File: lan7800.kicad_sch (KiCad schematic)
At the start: 31 parts

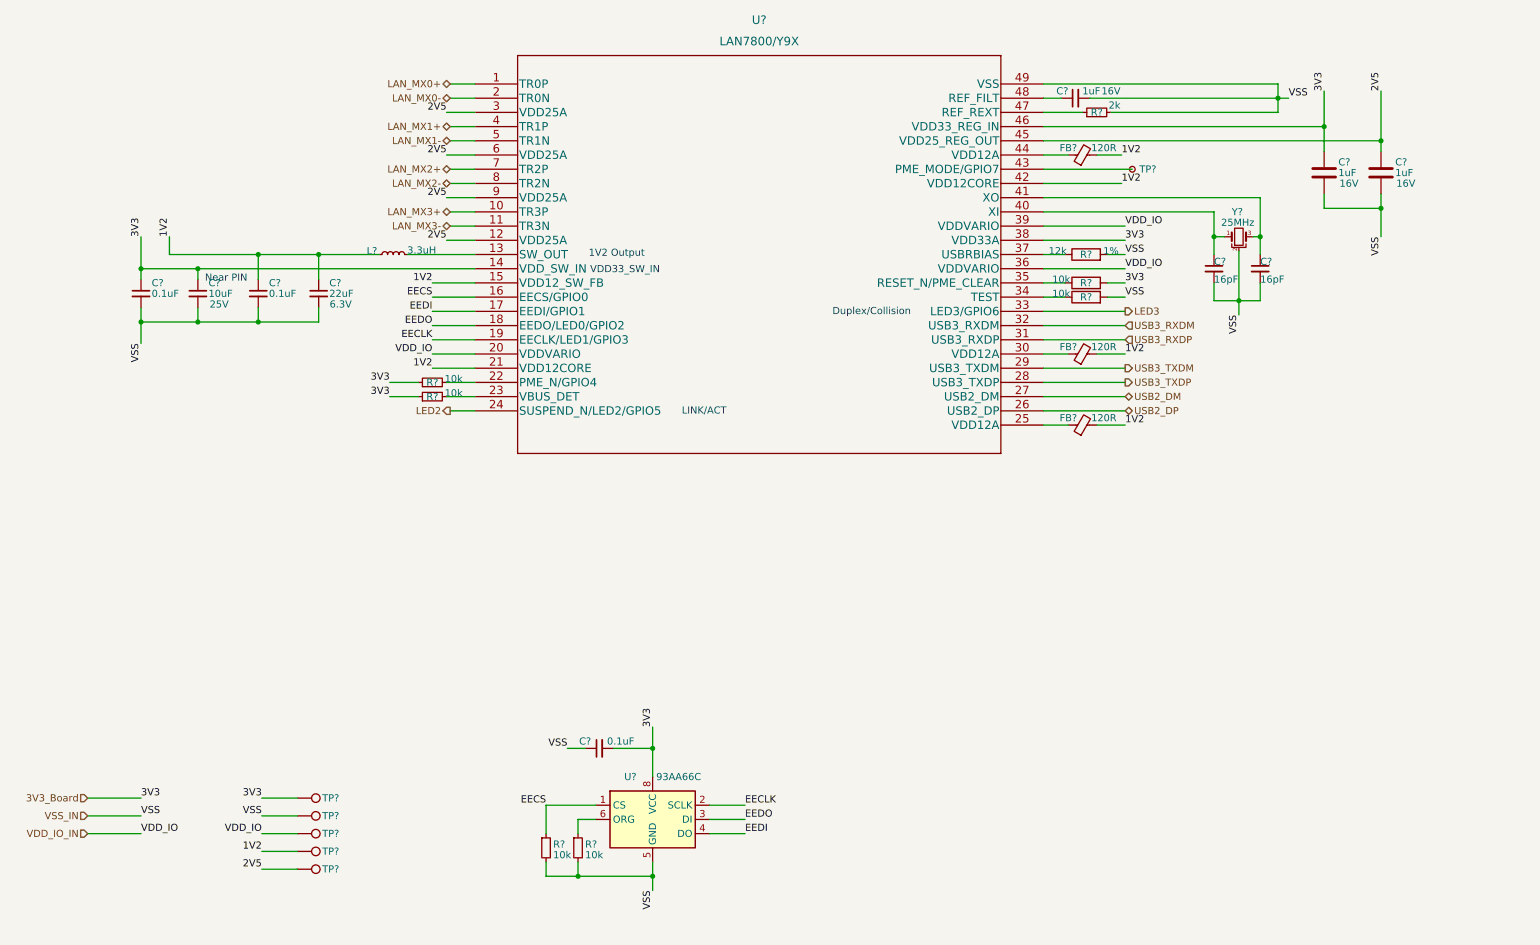
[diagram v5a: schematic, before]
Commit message: finished lm5116 circuit foot print assignment
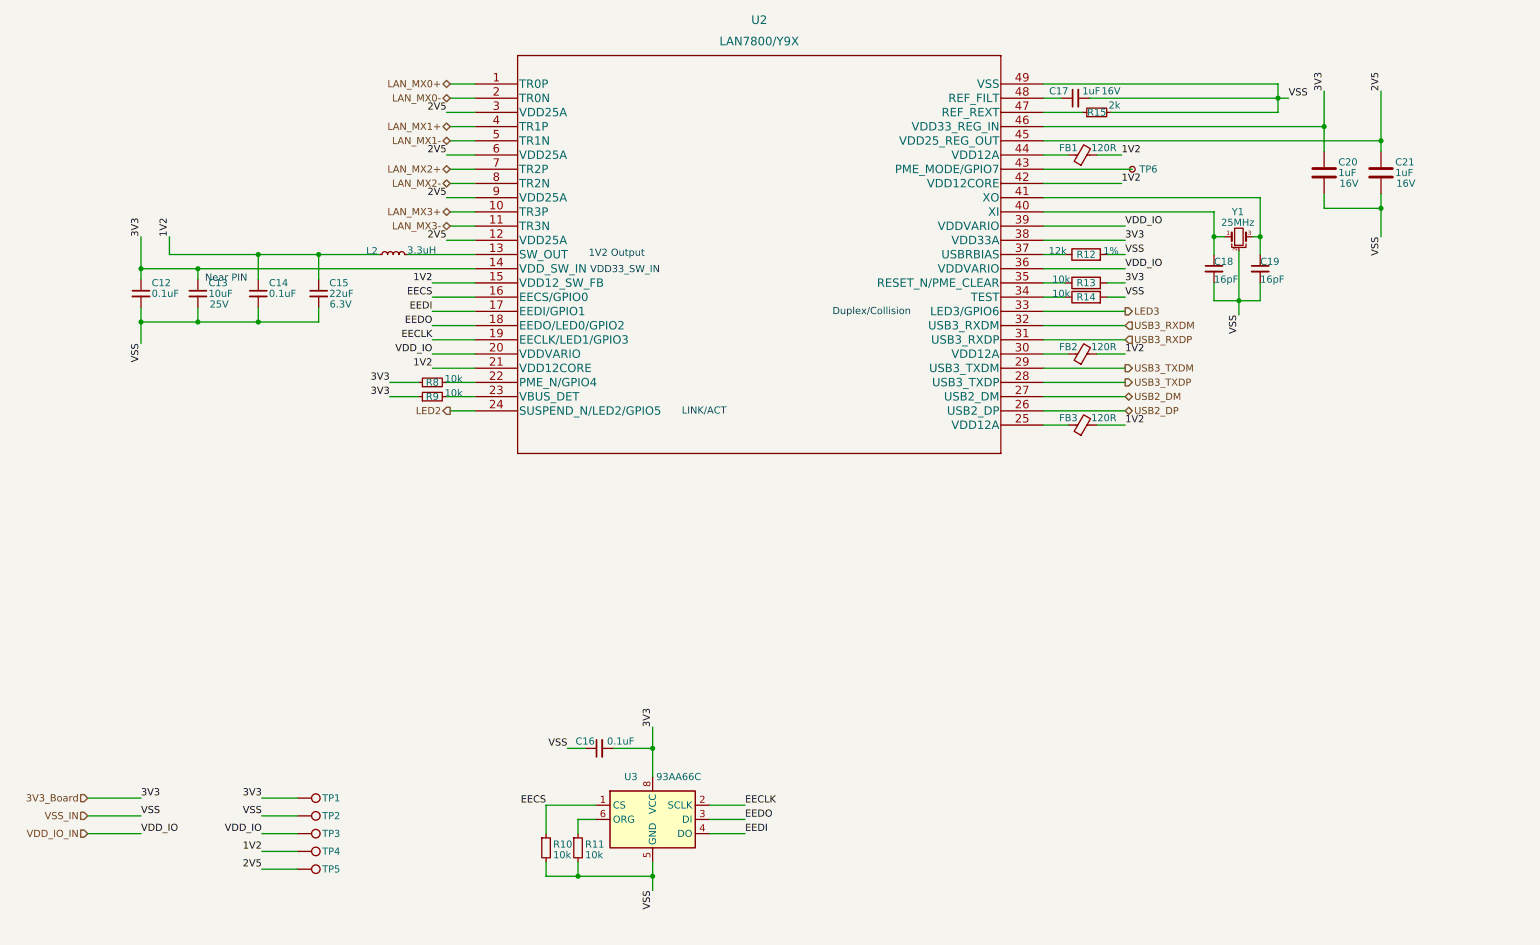
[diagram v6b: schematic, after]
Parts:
- gave numbers to parts that had none: 31
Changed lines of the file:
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@@
   (symbol (lib_id "Connector:TestPoint_Small") (at 211.455 48.895 0) (unit 1)
     (in_bom yes) (on_board yes)
-    (property "Reference" "TP?" (id 0) (at 212.725 48.895 0)
+    (property "Reference" "TP6" (id 0) (at 212.725 48.895 0)
       (effects (font (size 1.27 1.27)) (justify left))
     )
@@
   (symbol (lib_id "Memory_EEPROM:93AAxxC") (at 125.73 165.1 0) (unit 1)
     (in_bom yes) (on_board yes)
-    (property "Reference" "U?" (id 0) (at 120.65 157.48 0)
+    (property "Reference" "U3" (id 0) (at 120.65 157.48 0)
       (effects (font (size 1.27 1.27)) (justify left))
     )
@@
   (symbol (lib_id "Device:FerriteBead_Small") (at 202.565 46.355 90) (unit 1)
     (in_bom yes) (on_board yes)
-    (property "Reference" "FB?" (id 0) (at 200.025 45.085 90))
+    (property "Reference" "FB1" (id 0) (at 200.025 45.085 90))
     (property "Value" "120R" (id 1) (at 206.375 45.085 90))
     (property "Footprint" "" (id 2) (at 202.565 48.133 90)
@@
   (symbol (lib_id "Connector:TestPoint") (at 62.23 161.29 270) (unit 1)
     (in_bom yes) (on_board yes)
-    (property "Reference" "TP?" (id 0) (at 66.675 161.29 90)
+    (property "Reference" "TP1" (id 0) (at 66.675 161.29 90)
       (effects (font (size 1.27 1.27)) (justify left))
     )
@@
   (symbol (lib_id "Device:C_Small") (at 226.06 66.675 0) (unit 1)
     (in_bom yes) (on_board yes)
-    (property "Reference" "C?" (id 0) (at 226.06 65.405 0)
+    (property "Reference" "C18" (id 0) (at 226.06 65.405 0)
       (effects (font (size 1.27 1.27)) (justify left))
     )
@@
   (symbol (lib_id "Device:L_Small") (at 79.375 64.135 90) (unit 1)
     (in_bom yes) (on_board yes)
-    (property "Reference" "L?" (id 0) (at 75.565 63.5 90))
+    (property "Reference" "L2" (id 0) (at 75.565 63.5 90))
     (property "Value" "3.3uH" (id 1) (at 84.455 63.373 90))
     (property "Footprint" "" (id 2) (at 79.375 64.135 0)
@@
   (symbol (lib_id "Device:R") (at 203.2 69.215 90) (unit 1)
     (in_bom yes) (on_board yes)
-    (property "Reference" "R?" (id 0) (at 203.2 69.215 90))
+    (property "Reference" "R13" (id 0) (at 203.2 69.215 90))
     (property "Value" "10k" (id 1) (at 198.755 68.58 90))
     (property "Footprint" "" (id 2) (at 203.2 70.993 90)
@@
   (symbol (lib_id "Connector:TestPoint") (at 62.23 164.465 270) (unit 1)
     (in_bom yes) (on_board yes)
-    (property "Reference" "TP?" (id 0) (at 66.675 164.465 90)
+    (property "Reference" "TP2" (id 0) (at 66.675 164.465 90)
       (effects (font (size 1.27 1.27)) (justify left))
     )
@@
   (symbol (lib_id "Device:R") (at 203.2 64.135 90) (unit 1)
     (in_bom yes) (on_board yes)
-    (property "Reference" "R?" (id 0) (at 203.2 64.135 90))
+    (property "Reference" "R12" (id 0) (at 203.2 64.135 90))
     (property "Value" "12k" (id 1) (at 198.12 63.5 90))
     (property "Footprint" "" (id 2) (at 203.2 65.913 90)
@@
   (symbol (lib_id "Device:FerriteBead_Small") (at 202.565 81.915 90) (unit 1)
     (in_bom yes) (on_board yes)
-    (property "Reference" "FB?" (id 0) (at 200.025 80.645 90))
+    (property "Reference" "FB2" (id 0) (at 200.025 80.645 90))
     (property "Value" "120R" (id 1) (at 206.375 80.645 90))
     (property "Footprint" "" (id 2) (at 202.565 83.693 90)
@@
   (symbol (lib_id "Device:C_Small") (at 44.45 71.12 0) (unit 1)
     (in_bom yes) (on_board yes)
-    (property "Reference" "C?" (id 0) (at 46.355 69.215 0)
+    (property "Reference" "C13" (id 0) (at 46.355 69.215 0)
       (effects (font (size 1.27 1.27)) (justify left))
     )
@@
   (symbol (lib_id "Device:R_Small") (at 86.36 89.535 90) (unit 1)
     (in_bom yes) (on_board yes)
-    (property "Reference" "R?" (id 0) (at 86.36 89.535 90))
+    (property "Reference" "R9" (id 0) (at 86.36 89.535 90))
     (property "Value" "10k" (id 1) (at 90.17 88.9 90))
     (property "Footprint" "" (id 2) (at 86.36 89.535 0)
@@
   (symbol (lib_id "Connector:TestPoint") (at 62.23 173.99 270) (unit 1)
     (in_bom yes) (on_board yes)
-    (property "Reference" "TP?" (id 0) (at 66.675 173.99 90)
+    (property "Reference" "TP5" (id 0) (at 66.675 173.99 90)
       (effects (font (size 1.27 1.27)) (justify left))
     )
@@
   (symbol (lib_id "Device:C_Small") (at 34.29 71.12 0) (unit 1)
     (in_bom yes) (on_board yes)
-    (property "Reference" "C?" (id 0) (at 36.195 69.215 0)
+    (property "Reference" "C12" (id 0) (at 36.195 69.215 0)
       (effects (font (size 1.27 1.27)) (justify left))
     )
@@
   (symbol (lib_id "Device:C_Small") (at 66.04 71.12 0) (unit 1)
     (in_bom yes) (on_board yes)
-    (property "Reference" "C?" (id 0) (at 67.945 69.215 0)
+    (property "Reference" "C15" (id 0) (at 67.945 69.215 0)
       (effects (font (size 1.27 1.27)) (justify left))
     )
@@
   (symbol (lib_id "Connector:TestPoint") (at 62.23 167.64 270) (unit 1)
     (in_bom yes) (on_board yes)
-    (property "Reference" "TP?" (id 0) (at 66.675 167.64 90)
+    (property "Reference" "TP3" (id 0) (at 66.675 167.64 90)
       (effects (font (size 1.27 1.27)) (justify left))
     )
@@
   (symbol (lib_id "Device:FerriteBead_Small") (at 202.565 94.615 90) (unit 1)
     (in_bom yes) (on_board yes)
-    (property "Reference" "FB?" (id 0) (at 200.025 93.345 90))
+    (property "Reference" "FB3" (id 0) (at 200.025 93.345 90))
     (property "Value" "120R" (id 1) (at 206.375 93.345 90))
     (property "Footprint" "" (id 2) (at 202.565 96.393 90)
@@
   (symbol (lib_id "Device:R_Small") (at 86.36 86.995 90) (unit 1)
     (in_bom yes) (on_board yes)
-    (property "Reference" "R?" (id 0) (at 86.36 86.995 90))
+    (property "Reference" "R8" (id 0) (at 86.36 86.995 90))
     (property "Value" "10k" (id 1) (at 90.17 86.36 90))
     (property "Footprint" "" (id 2) (at 86.36 86.995 0)
@@
   (symbol (lib_id "Device:C") (at 245.745 49.53 0) (unit 1)
     (in_bom yes) (on_board yes)
-    (property "Reference" "C?" (id 0) (at 248.285 47.625 0)
+    (property "Reference" "C20" (id 0) (at 248.285 47.625 0)
       (effects (font (size 1.27 1.27)) (justify left))
     )
@@
   (symbol (lib_id "Device:R_Small") (at 205.105 38.735 90) (unit 1)
     (in_bom yes) (on_board yes)
-    (property "Reference" "R?" (id 0) (at 205.105 38.735 90))
+    (property "Reference" "R15" (id 0) (at 205.105 38.735 90))
     (property "Value" "2k" (id 1) (at 208.28 37.465 90))
     (property "Footprint" "" (id 2) (at 205.105 38.735 0)
@@
   (symbol (lib_id "Device:C_Small") (at 201.295 36.195 90) (unit 1)
     (in_bom yes) (on_board yes)
-    (property "Reference" "C?" (id 0) (at 200.025 34.925 90)
+    (property "Reference" "C17" (id 0) (at 200.025 34.925 90)
       (effects (font (size 1.27 1.27)) (justify left))
     )
@@
   (symbol (lib_id "Device:C") (at 255.905 49.53 0) (unit 1)
     (in_bom yes) (on_board yes)
-    (property "Reference" "C?" (id 0) (at 258.445 47.625 0)
+    (property "Reference" "C21" (id 0) (at 258.445 47.625 0)
       (effects (font (size 1.27 1.27)) (justify left))
     )
@@
   (symbol (lib_id "Device:C_Small") (at 55.245 71.12 0) (unit 1)
     (in_bom yes) (on_board yes)
-    (property "Reference" "C?" (id 0) (at 57.15 69.215 0)
+    (property "Reference" "C14" (id 0) (at 57.15 69.215 0)
       (effects (font (size 1.27 1.27)) (justify left))
     )
@@
   (symbol (lib_id "Device:Crystal_GND2_Small") (at 230.505 60.96 0) (unit 1)
     (in_bom yes) (on_board yes)
-    (property "Reference" "Y?" (id 0) (at 229.235 56.515 0)
+    (property "Reference" "Y1" (id 0) (at 229.235 56.515 0)
       (effects (font (size 1.27 1.27)) (justify left))
     )
@@
   (symbol (lib_id "Device:C_Small") (at 116.205 152.4 90) (unit 1)
     (in_bom yes) (on_board yes)
-    (property "Reference" "C?" (id 0) (at 113.665 151.13 90))
+    (property "Reference" "C16" (id 0) (at 113.665 151.13 90))
     (property "Value" "0.1uF" (id 1) (at 120.015 151.13 90))
     (property "Footprint" "" (id 2) (at 116.205 152.4 0)
@@
   (symbol (lib_id "Connector:TestPoint") (at 62.23 170.815 270) (unit 1)
     (in_bom yes) (on_board yes)
-    (property "Reference" "TP?" (id 0) (at 66.675 170.815 90)
+    (property "Reference" "TP4" (id 0) (at 66.675 170.815 90)
       (effects (font (size 1.27 1.27)) (justify left))
     )
@@
   (symbol (lib_id "Device:R") (at 203.2 71.755 90) (unit 1)
     (in_bom yes) (on_board yes)
-    (property "Reference" "R?" (id 0) (at 203.2 71.755 90))
+    (property "Reference" "R14" (id 0) (at 203.2 71.755 90))
     (property "Value" "10k" (id 1) (at 198.755 71.12 90))
     (property "Footprint" "" (id 2) (at 203.2 73.533 90)
@@
   (symbol (lib_id "Device:C_Small") (at 234.315 66.675 0) (unit 1)
     (in_bom yes) (on_board yes)
-    (property "Reference" "C?" (id 0) (at 234.315 65.405 0)
+    (property "Reference" "C19" (id 0) (at 234.315 65.405 0)
       (effects (font (size 1.27 1.27)) (justify left))
     )
@@
   (symbol (lib_id "LAN7800:LAN7800{slash}Y9X") (at 93.98 33.655 0) (unit 1)
     (in_bom yes) (on_board yes) (fields_autoplaced)
-    (property "Reference" "U?" (id 0) (at 144.78 22.225 0)
+    (property "Reference" "U2" (id 0) (at 144.78 22.225 0)
       (effects (font (size 1.524 1.524)))
     )
@@
   (symbol (lib_id "Device:R_Small") (at 112.395 170.18 0) (unit 1)
     (in_bom yes) (on_board yes)
-    (property "Reference" "R?" (id 0) (at 113.665 169.545 0)
+    (property "Reference" "R11" (id 0) (at 113.665 169.545 0)
       (effects (font (size 1.27 1.27)) (justify left))
     )
@@
   (symbol (lib_id "Device:R_Small") (at 106.68 170.18 0) (unit 1)
     (in_bom yes) (on_board yes)
-    (property "Reference" "R?" (id 0) (at 107.95 169.545 0)
-      (effects (font (size 1.27 1.27)) (justify left))
-    )
+    (property "Reference" "R10" (id 0) (at 107.95 169.545 0)
+      (effects (font (size 1.27 1.27)) (justify left))
+    )

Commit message: PoE Library Update
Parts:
- C16: footprint (none) -> Capacitor_SMD:C_0201_0603Metric; now left out of the parts list
- R10, R11: footprint (none) -> Resistor_SMD:R_0201_0603Metric; now left out of the parts list
- U2: footprint SQFN48_7X7_Y9X_MCH -> Package_DFN_QFN:QFN-48-1EP_7x7mm_P0.5mm_EP5.3x5.3mm
- U3: footprint (none) -> Package_SO:SOIC-8-1EP_3.9x4.9mm_P1.27mm_EP2.29x3mm; now left out of the parts list
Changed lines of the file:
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@@
   )
   (symbol (lib_id "Memory_EEPROM:93AAxxC") (at 125.73 165.1 0) (unit 1)
-    (in_bom yes) (on_board yes)
+    (in_bom no) (on_board yes)
     (property "Reference" "U3" (id 0) (at 120.65 157.48 0)
       (effects (font (size 1.27 1.27)) (justify left))
@@
       (effects (font (size 1.27 1.27)) (justify left))
     )
-    (property "Footprint" "" (id 2) (at 125.73 165.1 0)
+    (property "Footprint" "Package_SO:SOIC-8-1EP_3.9x4.9mm_P1.27mm_EP2.29x3mm" (id 2) (at 125.73 165.1 0)
       (effects (font (size 1.27 1.27)) hide)
     )
@@
   )
   (symbol (lib_id "Device:C_Small") (at 116.205 152.4 90) (unit 1)
-    (in_bom yes) (on_board yes)
+    (in_bom no) (on_board yes)
     (property "Reference" "C16" (id 0) (at 113.665 151.13 90))
     (property "Value" "0.1uF" (id 1) (at 120.015 151.13 90))
-    (property "Footprint" "" (id 2) (at 116.205 152.4 0)
+    (property "Footprint" "Capacitor_SMD:C_0201_0603Metric" (id 2) (at 116.205 152.4 0)
       (effects (font (size 1.27 1.27)) hide)
     )
@@
       (effects (font (size 1.524 1.524)))
     )
-    (property "Footprint" "SQFN48_7X7_Y9X_MCH" (id 2) (at 144.78 27.559 0)
+    (property "Footprint" "Package_DFN_QFN:QFN-48-1EP_7x7mm_P0.5mm_EP5.3x5.3mm" (id 2) (at 144.78 27.559 0)
       (effects (font (size 1.524 1.524)) hide)
     )
@@
   )
   (symbol (lib_id "Device:R_Small") (at 112.395 170.18 0) (unit 1)
-    (in_bom yes) (on_board yes)
+    (in_bom no) (on_board yes)
     (property "Reference" "R11" (id 0) (at 113.665 169.545 0)
       (effects (font (size 1.27 1.27)) (justify left))
@@
       (effects (font (size 1.27 1.27)) (justify left))
     )
-    (property "Footprint" "" (id 2) (at 112.395 170.18 0)
+    (property "Footprint" "Resistor_SMD:R_0201_0603Metric" (id 2) (at 112.395 170.18 0)
       (effects (font (size 1.27 1.27)) hide)
     )
@@
   )
   (symbol (lib_id "Device:R_Small") (at 106.68 170.18 0) (unit 1)
-    (in_bom yes) (on_board yes)
+    (in_bom no) (on_board yes)
     (property "Reference" "R10" (id 0) (at 107.95 169.545 0)
       (effects (font (size 1.27 1.27)) (justify left))
@@
       (effects (font (size 1.27 1.27)) (justify left))
     )
-    (property "Footprint" "" (id 2) (at 106.68 170.18 0)
-      (effects (font (size 1.27 1.27)) hide)
-    )
+    (property "Footprint" "Resistor_SMD:R_0201_0603Metric" (id 2) (at 106.68 170.18 0)
+      (effects (font (size 1.27 1.27)) hide)
+    )

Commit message: Footprint without TPS2372
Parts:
- C12: footprint (none) -> Capacitor_SMD:C_0603_1608Metric; Voltage (none) -> https://item.szlcsc.com/1942.html
- C13, C14, C15, C17, C18, C19, C20, C21: footprint (none) -> Capacitor_SMD:C_0603_1608Metric
- C16: footprint Capacitor_SMD:C_0201_0603Metric -> Capacitor_SMD:C_0603_1608Metric
- FB1: footprint (none) -> Inductor_SMD:L_0603_1608Metric
- FB2, FB3, R12, R13, R14, R15, R8, R9: footprint (none) -> Resistor_SMD:R_0603_1608Metric
- L2: footprint (none) -> Inductor_SMD:L_1206_3216Metric
- R10, R11: footprint Resistor_SMD:R_0201_0603Metric -> Resistor_SMD:R_0603_1608Metric
- U2: footprint Package_DFN_QFN:QFN-48-1EP_7x7mm_P0.5mm_EP5.3x5.3mm -> PoE_Devices:LAN7800&slash_Y9X
- Y1: footprint (none) -> Crystal:Crystal_SMD_3225-4Pin_3.2x2.5mm
